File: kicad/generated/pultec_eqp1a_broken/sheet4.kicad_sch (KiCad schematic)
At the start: 14 parts, among them T2 core

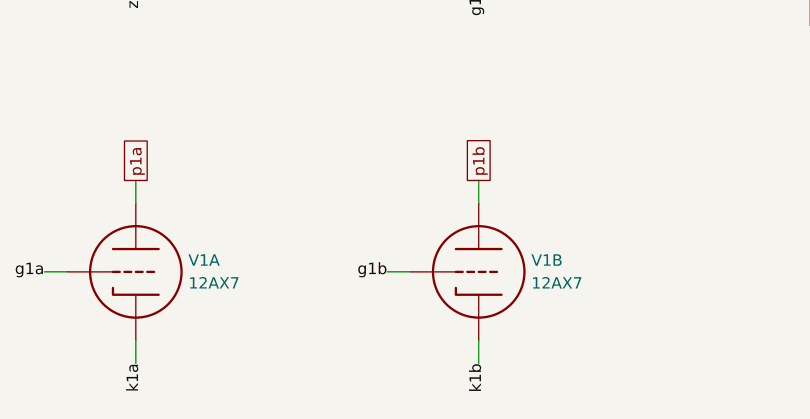
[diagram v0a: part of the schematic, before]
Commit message: Component editor C1: device files are pinned component versions
Device files move to config/components/<name>/<N>.yaml (the twelve former
config/devices/*.yaml are version 1, bytes unchanged), each version's sha256
(LF-normalized) in config/components/versions.lock. varimu/devices/versions.py
and varimu-circuit's versions.rs read the store the same way: a version edited
after saving is a load error, a bare name is the latest version for tools and
tests, and both builders refuse a bare name in a circuit. Circuits pin NAME@N:
the hand-written circuits, their device-choice parameters, the drawn circuits,
the symbol table's and both editors' placement defaults, the KiCad fixtures.
varimu fit-devices saves a new version only when a fit changed. The native
editor's model picker lists every version.

Every circuit builds identical IR and SPICE (export_circuit_fixtures --golden,
export_app_fixtures without a diff); the editor fixtures change only by the
pins. Tests: tests/test_versions.py, crates/varimu-circuit/tests/versions.rs,
editor_draw.rs (swapping a pinned version rebuilds; undo).

Co-Authored-By: Claude Opus 5.5 (1M context) <noreply@anthropic.com>
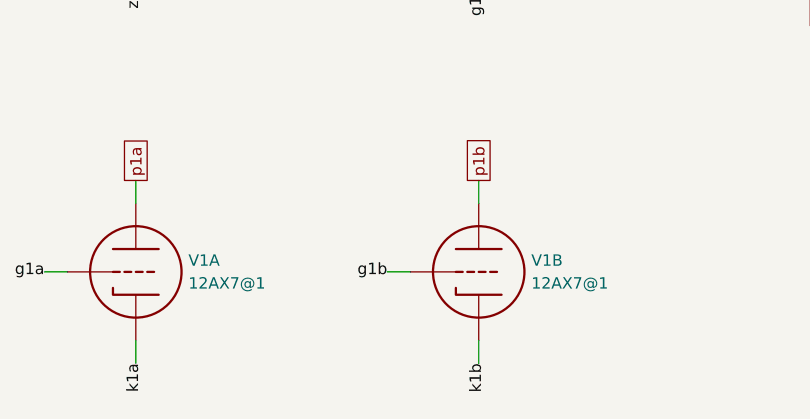
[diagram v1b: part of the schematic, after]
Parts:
- V1: value 12AX7 -> 12AX7@1
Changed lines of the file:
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@@
 			)
 		)
-		(property "Value" "12AX7"
+		(property "Value" "12AX7@1"
 			(at 196.342 77.47 0)
 			(effects
@@
 			)
 		)
-		(property "Value" "12AX7"
+		(property "Value" "12AX7@1"
 			(at 234.442 77.47 0)
 			(effects
